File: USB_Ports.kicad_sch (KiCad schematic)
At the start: 34 parts, among them IC2 TPS2066TDGNRQ1, IC3 TPS2066TDGNRQ1, J10 M8 USB Conn, J5 M8 USB Conn, J6 M8 USB Conn, J8 M8 USB Conn, U6 TPD4EUSB30, U7 TPD4EUSB30

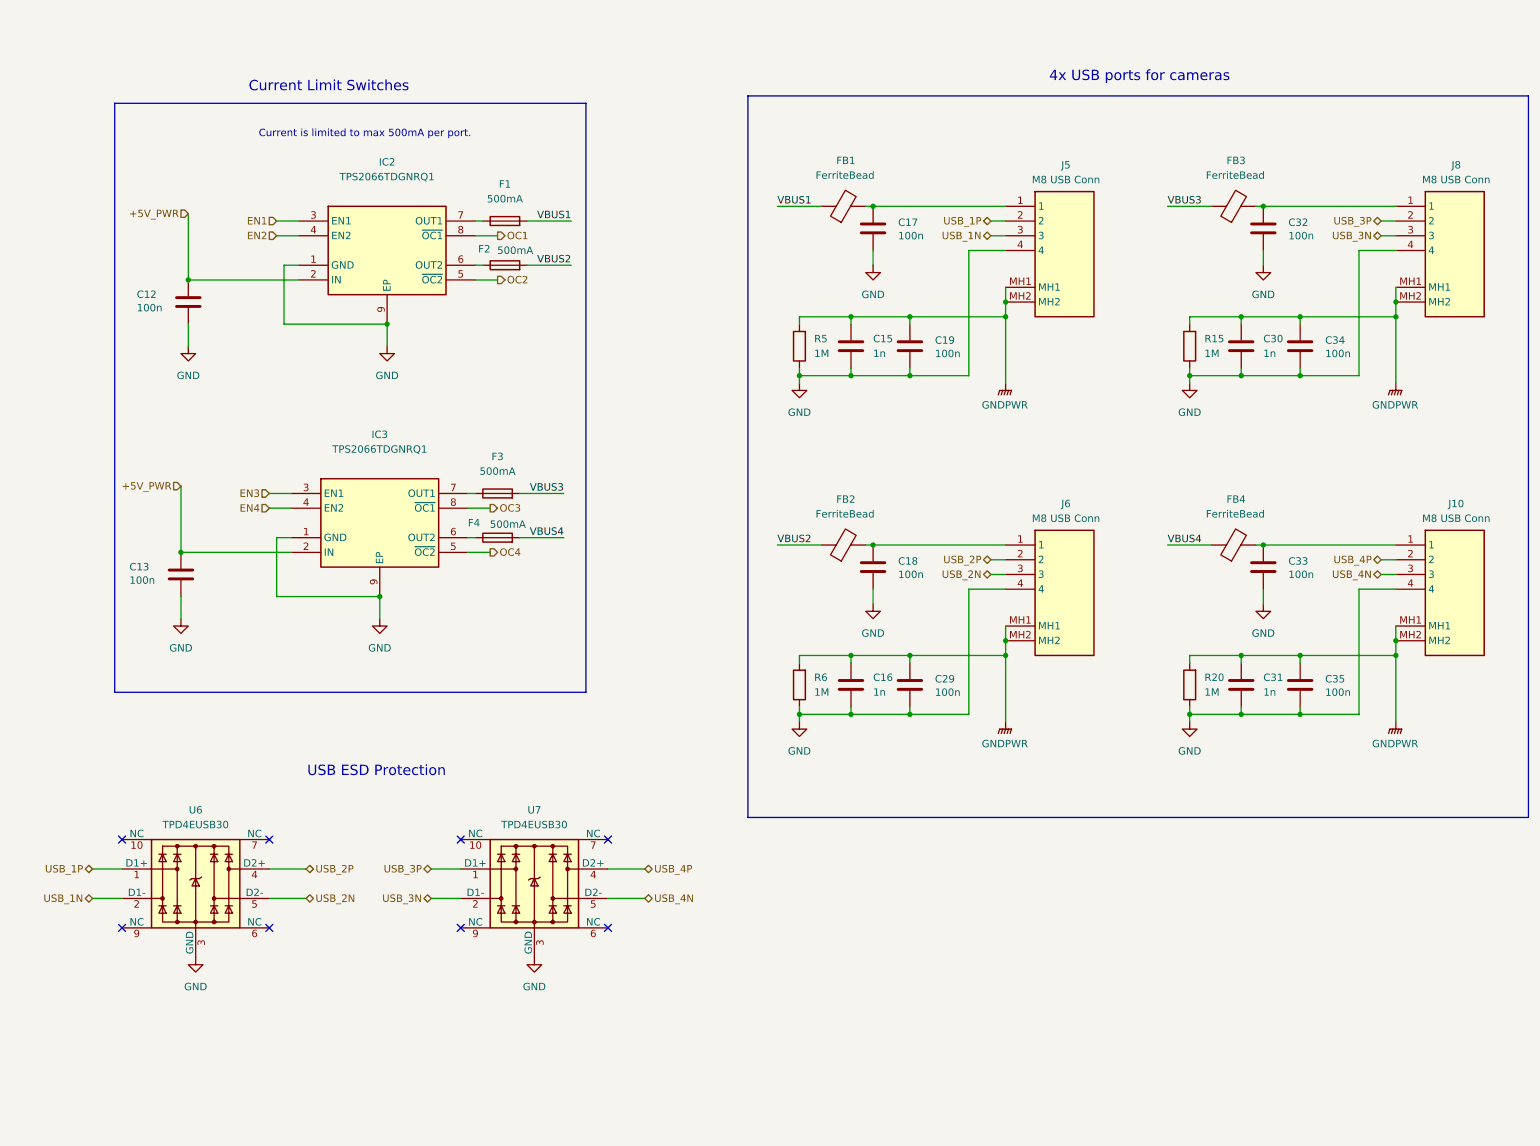
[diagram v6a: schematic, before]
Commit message: Migrate to USB C and added some ESD protections on Vbus; might still have some issues
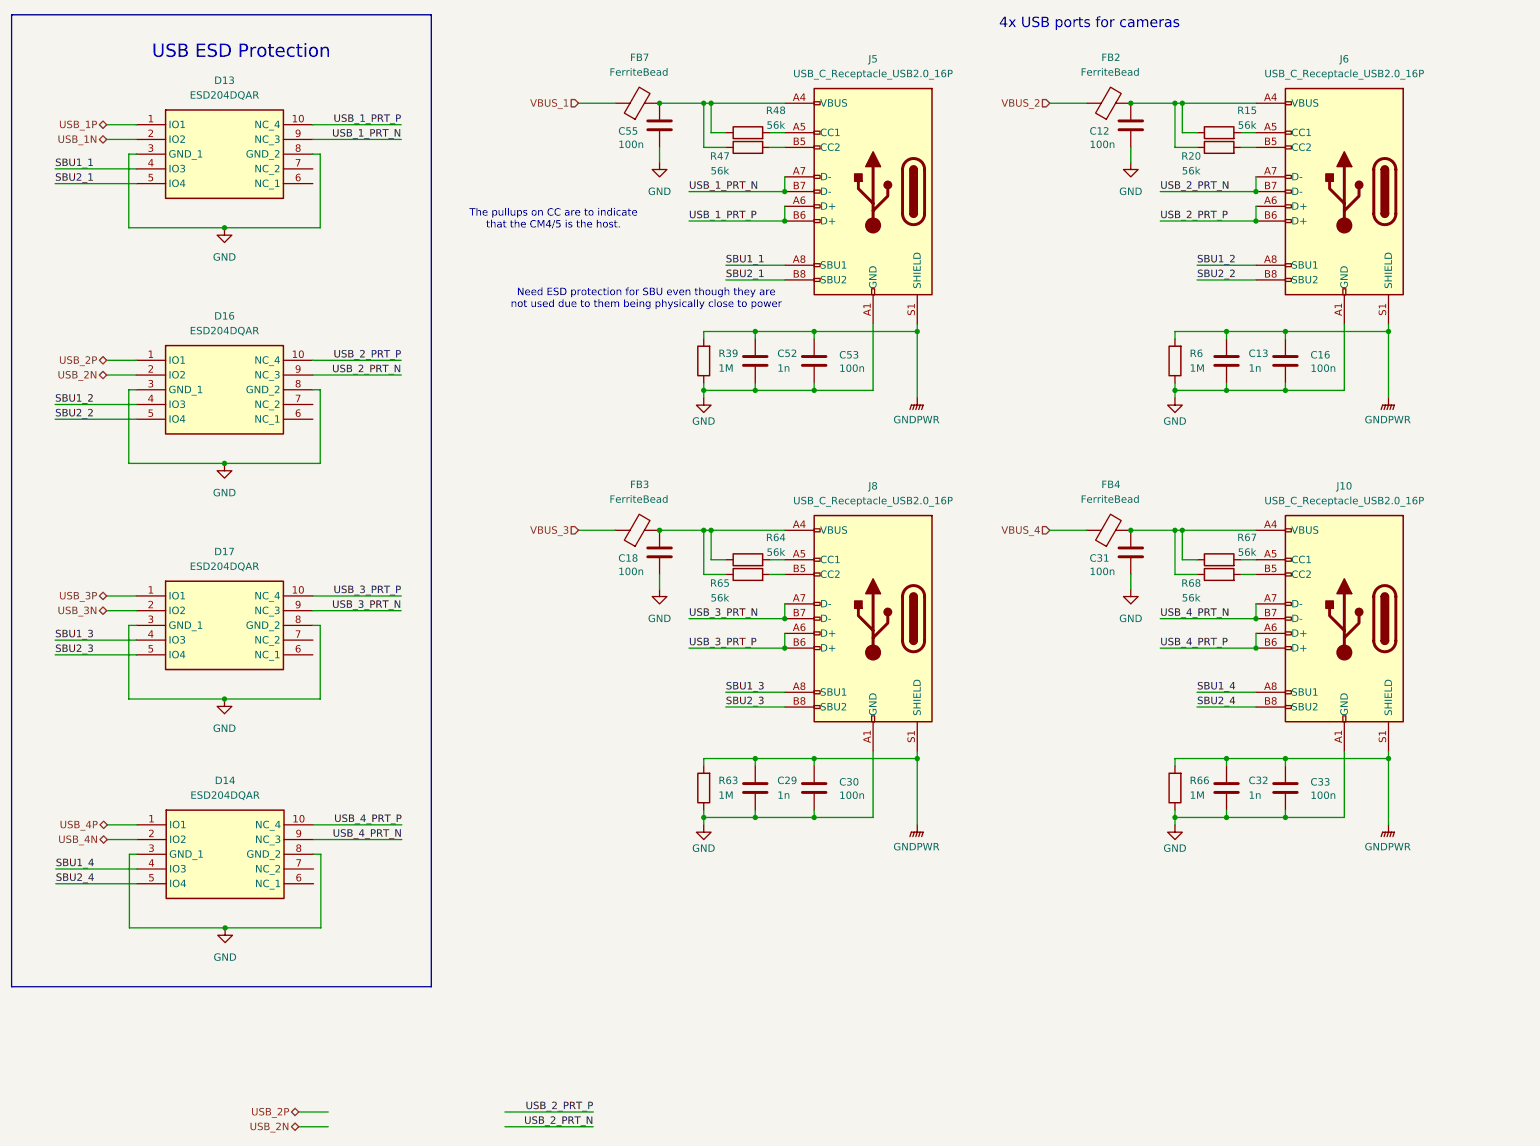
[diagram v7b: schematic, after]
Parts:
- removed C15: 1n, Capacitor_SMD:C_0805_2012Metric, symbol Device:C
- removed C17, C19, C34, C35: 100n, Capacitor_SMD:C_0805_2012Metric, symbol Device:C
- removed F1, F2, F3, F4: 500mA, Fuse:Fuse_1206_3216Metric, symbol Device:Fuse
- removed FB1: FerriteBead, Inductor_SMD:L_1206_3216Metric, symbol Device:FerriteBead
- removed IC2, IC3: TPS2066TDGNRQ1, Controls_Pi:SOP65P490X110-9N, symbol TPS2066TDGNRQ1:TPS2066TDGNRQ1
- removed J10, J5, J6, J8: M8 USB Conn, Controls_Pi:321720912, symbol 3-2172091-2:3-2172091-2
- removed R5: 1M, Resistor_SMD:R_0805_2012Metric, symbol Device:R
- removed U6, U7: TPD4EUSB30, Package_SON:USON-10_2.5x1.0mm_P0.5mm, symbol Power_Protection:TPD4EUSB30
- added C52: 1n, Capacitor_SMD:C_0805_2012Metric, symbol Device:C
- added C53, C55: 100n, Capacitor_SMD:C_0805_2012Metric, symbol Device:C
- added D13, D14, D16, D17: ESD204DQAR, Controls_Pi:ESD204DQAR, symbol ESD204DQAR:ESD204DQAR
- added FB7: FerriteBead, Inductor_SMD:L_1206_3216Metric, symbol Device:FerriteBead
- added J10, J5, J6, J8: USB_C_Receptacle_USB2.0_16P, symbol Connector:USB_C_Receptacle_USB2.0_16P
- added R39, R63, R66: 1M, Resistor_SMD:R_0805_2012Metric, symbol Device:R
- added R47, R48, R64, R65, R67, R68: 56k, Resistor_SMD:R_0805_2012Metric, symbol Device:R
- C13, C29, C32: value 100n -> 1n; P/N C0805C104M5RACTU -> C0805C102J5HACAUTO
- C16, C30, C31: value 1n -> 100n; P/N C0805C102J5HACAUTO -> C0805C104M5RACTU
- R15, R20: value 1M -> 56k; P/N CRCW08051M00FKEA -> CRCW080556K0FKEAHP
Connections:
- net GND: now also C52.2, C53.2, C55.2, D13.3 (GND_1), D13.8 (GND_2), D14.3 (GND_1), D14.8 (GND_2), D16.3 (GND_1), D16.8 (GND_2), D17.3 (GND_1), D17.8 (GND_2), J10.A1 (GND), J10.A12 (GND), J10.B1 (GND), J10.B12 (GND), J5.A1 (GND), J5.A12 (GND), J5.B1 (GND), J5.B12 (GND), J6.A1 (GND), J6.A12 (GND), J6.B1 (GND), J6.B12 (GND), J8.A1 (GND), J8.A12 (GND), J8.B1 (GND), J8.B12 (GND), R39.1, R63.1, R66.1; no longer R15.1, R20.1
- net GNDPWR: now also C13.1, C32.1, C33.1, C52.1, C53.1, J10.S1 (SHIELD), J5.S1 (SHIELD), J6.S1 (SHIELD), J8.S1 (SHIELD), R39.2, R63.2, R66.2; no longer C31.1, R15.2, R20.2
- net USB_1N: now also D13.2 (IO2)
- net USB_1P: now also D13.1 (IO1)
- net USB_2N: now also D16.2 (IO2)
- net USB_2P: now also D16.1 (IO1)
- net USB_3N: now also D17.2 (IO2)
- net USB_3P: now also D17.1 (IO1)
- net USB_4N: now also D14.2 (IO2)
- net USB_4P: now also D14.1 (IO1)
- net at C18.1: now also FB3.2, J8.A4 (VBUS), J8.A9 (VBUS), J8.B4 (VBUS), J8.B9 (VBUS), R64.1, R65.1; no longer FB2.2
- net at FB4.2: now also C31.1, J10.A4 (VBUS), J10.A9 (VBUS), J10.B4 (VBUS), J10.B9 (VBUS), R67.1, R68.1; no longer C33.1
- net +5V_PWR: no longer names the net of C12.1
- net +5V_PWR: now also FB2.2, R15.1, R20.1, J6.A4 (VBUS), J6.A9 (VBUS), J6.B4 (VBUS), J6.B9 (VBUS); no longer C13.1
- net VBUS2 renamed VBUS_2
- net VBUS3 renamed VBUS_3
- net VBUS4 renamed VBUS_4
- new net: C55.1, FB7.2, J5.A4 (VBUS), J5.A9 (VBUS), J5.B4 (VBUS), J5.B9 (VBUS), R47.1, R48.1
- new net: J5.A5 (CC1), R48.2
- new net: J5.B5 (CC2), R47.2
- new net: J6.A5 (CC1), R15.2
- new net: J6.B5 (CC2), R20.2
- new net: J8.A5 (CC1), R64.2
- new net: J10.A5 (CC1), R67.2
- new net: J8.B5 (CC2), R65.2
- new net: J10.B5 (CC2), R68.2
- new net SBU1_1: D13.4 (IO3), J5.A8 (SBU1)
- new net SBU1_2: D16.4 (IO3), J6.A8 (SBU1)
- new net SBU1_3: D17.4 (IO3), J8.A8 (SBU1)
- new net SBU1_4: D14.4 (IO3), J10.A8 (SBU1)
- new net SBU2_1: D13.5 (IO4), J5.B8 (SBU2)
- new net SBU2_2: D16.5 (IO4), J6.B8 (SBU2)
- new net SBU2_3: D17.5 (IO4), J8.B8 (SBU2)
- new net SBU2_4: D14.5 (IO4), J10.B8 (SBU2)
- new net USB_1_PRT_N: D13.9 (NC_3), J5.A7 (D-), J5.B7 (D-)
- new net USB_1_PRT_P: D13.10 (NC_4), J5.A6 (D+), J5.B6 (D+)
- new net USB_2_PRT_N: D16.9 (NC_3), J6.A7 (D-), J6.B7 (D-)
- new net USB_2_PRT_P: D16.10 (NC_4), J6.A6 (D+), J6.B6 (D+)
- new net USB_3_PRT_N: D17.9 (NC_3), J8.A7 (D-), J8.B7 (D-)
- new net USB_3_PRT_P: D17.10 (NC_4), J8.A6 (D+), J8.B6 (D+)
- new net USB_4_PRT_N: D14.9 (NC_3), J10.A7 (D-), J10.B7 (D-)
- new net USB_4_PRT_P: D14.10 (NC_4), J10.A6 (D+), J10.B6 (D+)
- new net VBUS_1: FB7.1
- no-connect marks 8 -> 0
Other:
- note added: "Need ESD protection for SBU even though they are not used due to them being physically close to power"
- note added: "The pullups on CC are to indicate that the CM4/5 is the host."
- note removed: "Current Limit Switches"
- note removed: "Current is limited to max 500mA per port."

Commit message: fixed erc and removed old schematics
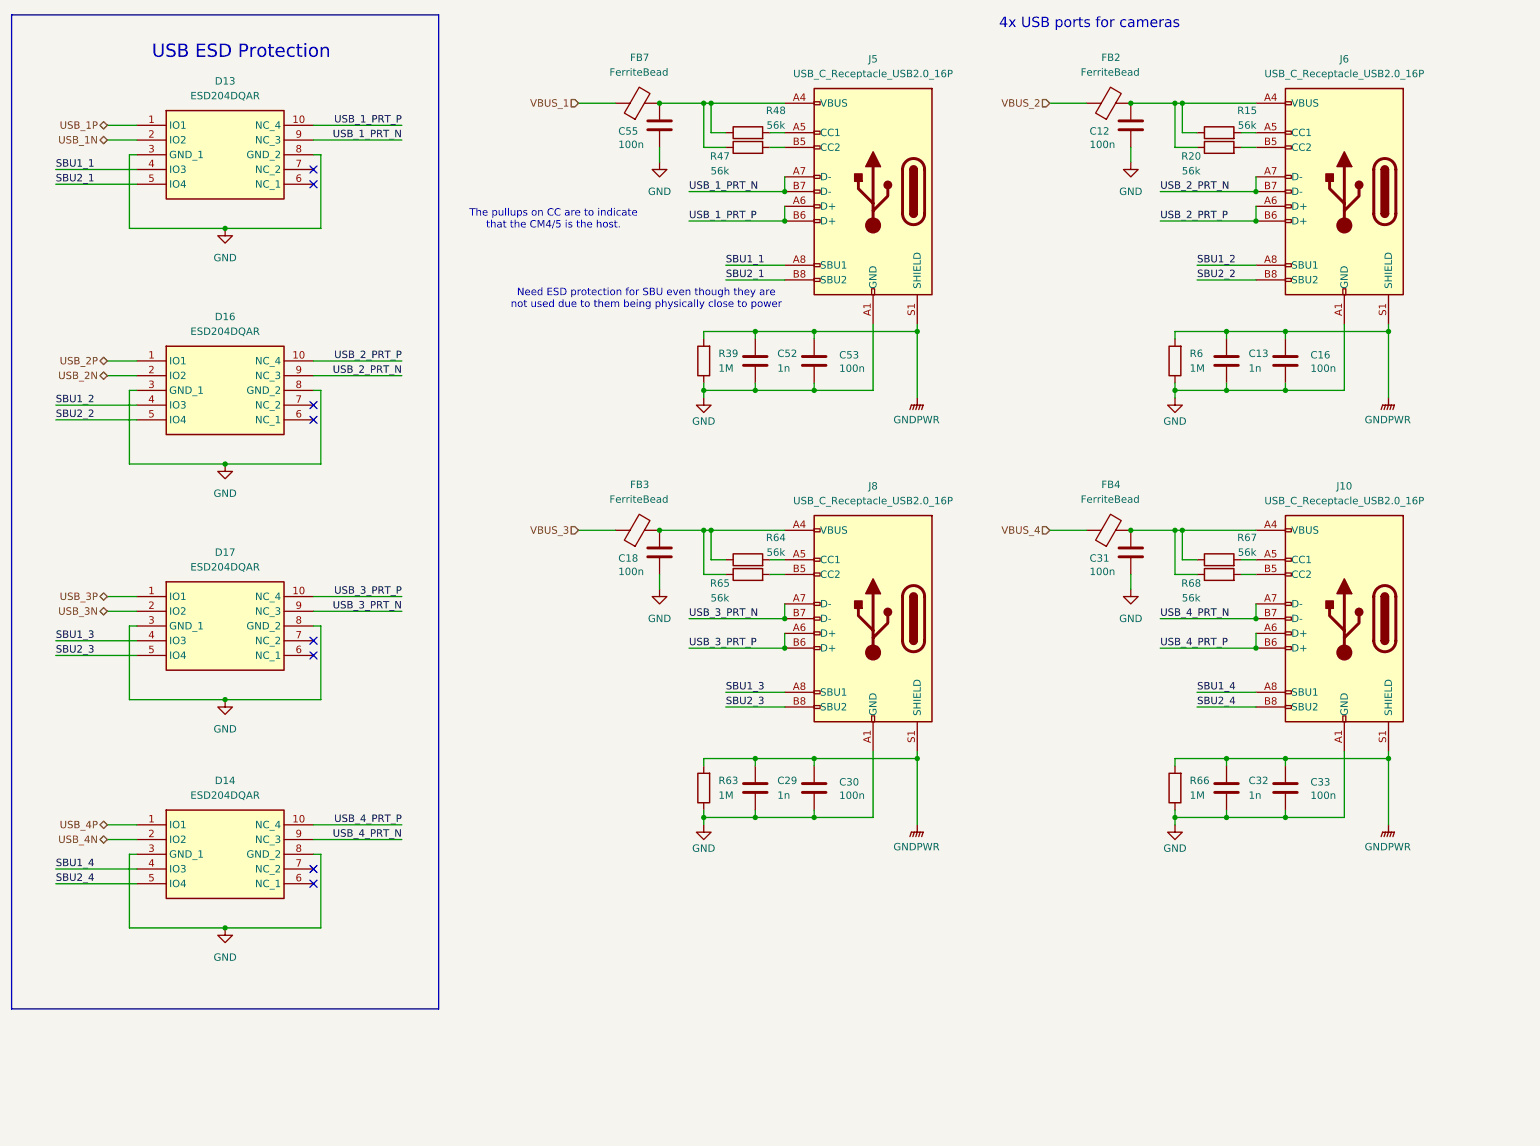
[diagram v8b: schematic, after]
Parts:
- D13, D14, D16, D17: Arrow Part Number (none) -> ESD204DQAR; Arrow Price/Stock (none) -> https://www.arrow.com/en/products/esd204dqar/texas-instrume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; Height (none) -> 0.55; Manufacturer_Name (none) -> Texas Instruments; Manufacturer_Part_Number (none) -> ESD204DQAR; Mouser Part Number (none) -> 595-ESD204DQAR; Mouser Price/Stock (none) -> https://www.mouser.co.uk/ProductDetail/Texas-Instruments/ES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
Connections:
- no-connect marks 0 -> 8
